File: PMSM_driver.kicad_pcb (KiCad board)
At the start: 2 copper layers, 81 parts, among them J1 22-23-2021, J2 302-S101, J3 Conn_Bridge_Power, J4 Conn_Phases, J5 Conn_Driver_Power, Q1 IRFH8334, Q2 IRFH8334, Q3 IRFH8334, Q4 IRFH8334, Q5 IRFH8334, Q6 IRFH8334, U1 IR2110, U2 IR2110, U3 IR2110, U4 LM358DT

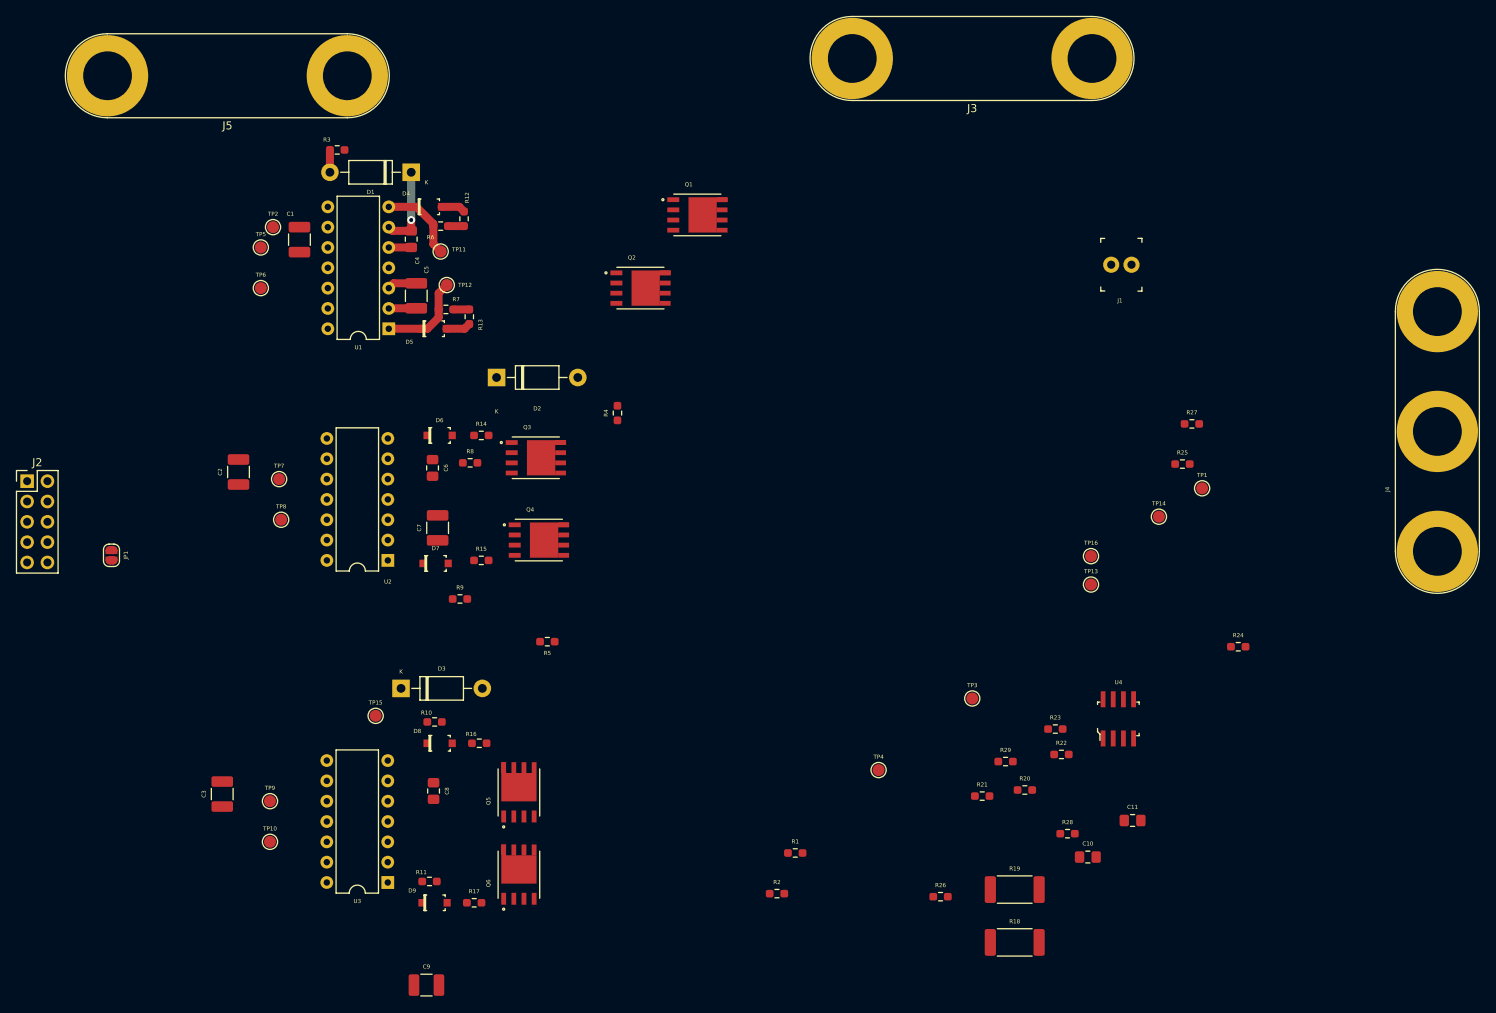
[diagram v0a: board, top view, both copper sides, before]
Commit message: [PCB]: components arrangment around 3 MOSFET drivers
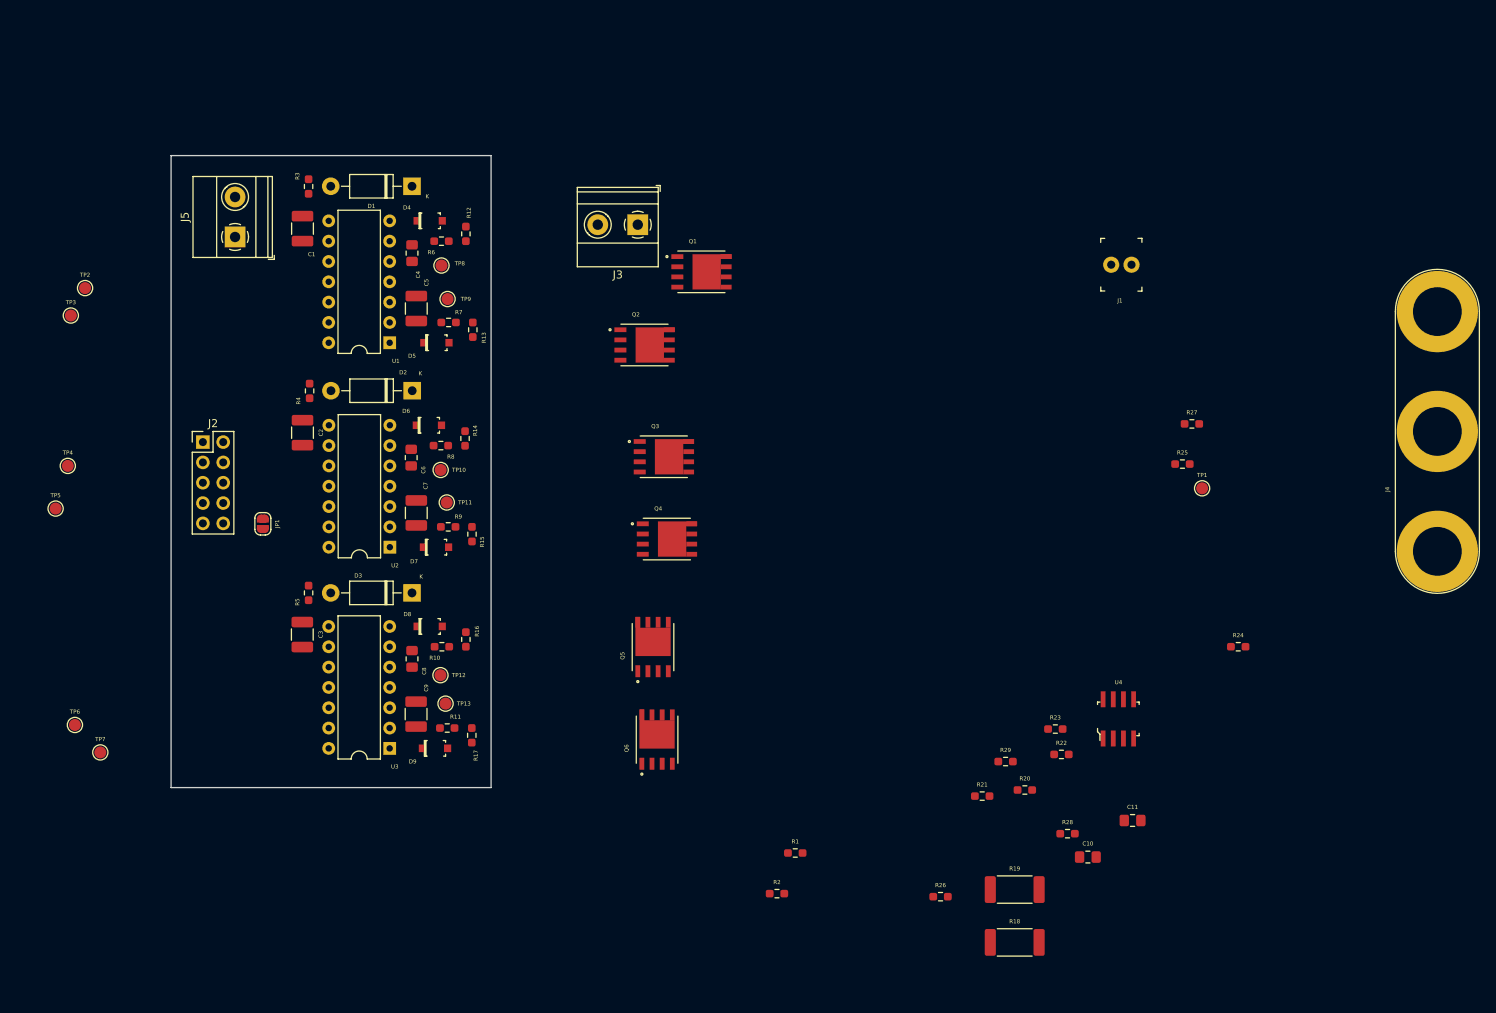
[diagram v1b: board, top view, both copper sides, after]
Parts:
- removed the TP2 at (110.7, 59.9)
- removed the TP3 at (198.2, 118.9)
- removed the TP4 at (186.4, 127.8)
- J3: value Conn_Bridge_Power -> Screw_Terminal_Power; footprint Connector:Banana_Jack_2Pin -> TerminalBlock_Phoenix:TerminalBlock_Phoenix_MKDS-1,5-2_1x02_P5.00mm_Horizontal
- J5: value Conn_Driver_Power -> Screw_Terminal_Logic; footprint Connector:Banana_Jack_2Pin -> TerminalBlock_Phoenix:TerminalBlock_Phoenix_MKDS-1,5-2_1x02_P5.00mm_Horizontal
- moved TP11 89.0 mm to (132.5, 94.4)
- moved TP13 82.8 mm to (132.3, 119.5)
- moved TP10 82.5 mm to (131.7, 90.3)
- moved J3 60.5 mm to (156.3, 59.6)
- moved R4 38.6 mm to (115.3, 80.4)
- moved C9 33.9 mm to (128.6, 120.8), turned to 90 degrees
- moved R5 30.5 mm to (115.2, 105.7), turned to 90 degrees
- moved TP5 28.2 mm to (83.6, 95.1)
- moved TP4 26.5 mm to (85.1, 89.8)
- moved TP6 26.2 mm to (86.0, 122.2)
- moved Q5 24.7 mm to (158.2, 112.4)
- moved J5 24.6 mm to (106.0, 61.2), turned to 90 degrees
- moved Q6 24.2 mm to (158.8, 124.0)
- moved TP3 24.0 mm to (85.5, 71.0)
- moved TP7 24.0 mm to (89.2, 125.6)
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- renumbered TP13 to TP10, TP14 to TP11, TP15 to TP12, TP16 to TP13, TP5 to TP2, TP6 to TP3, TP7 to TP4, TP8 to TP5, TP9 to TP6, TP10 to TP7, TP11 to TP8, TP12 to TP9
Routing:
- net Net-(D5-PadK): track 11.3 -> 0.00 mm
- net Net-(C4-Pad1): track 10.3 -> 0.00 mm, vias 1 -> 0
- net Net-(D4-PadK): track 10.3 -> 0.00 mm
- net VCC: track 3.69 -> 0.00 mm
- net GND: track 3.45 -> 0.00 mm
- net Net-(D5-PadA): track 3.11 -> 0.00 mm
- net Net-(D4-PadA): track 3.06 -> 0.00 mm
- net Net-(C4-Pad2): track 2.81 -> 0.00 mm
- net Net-(D1-Pad2): track 2.79 -> 0.00 mm
- net Net-(Q2-Pad4): track 2.01 -> 0.00 mm
- net Net-(Q1-Pad4): track 2.01 -> 0.00 mm
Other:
- board outline added: 40 x 79 mm

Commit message: [PCB]: added Power part of the board. Logic part rearrangement
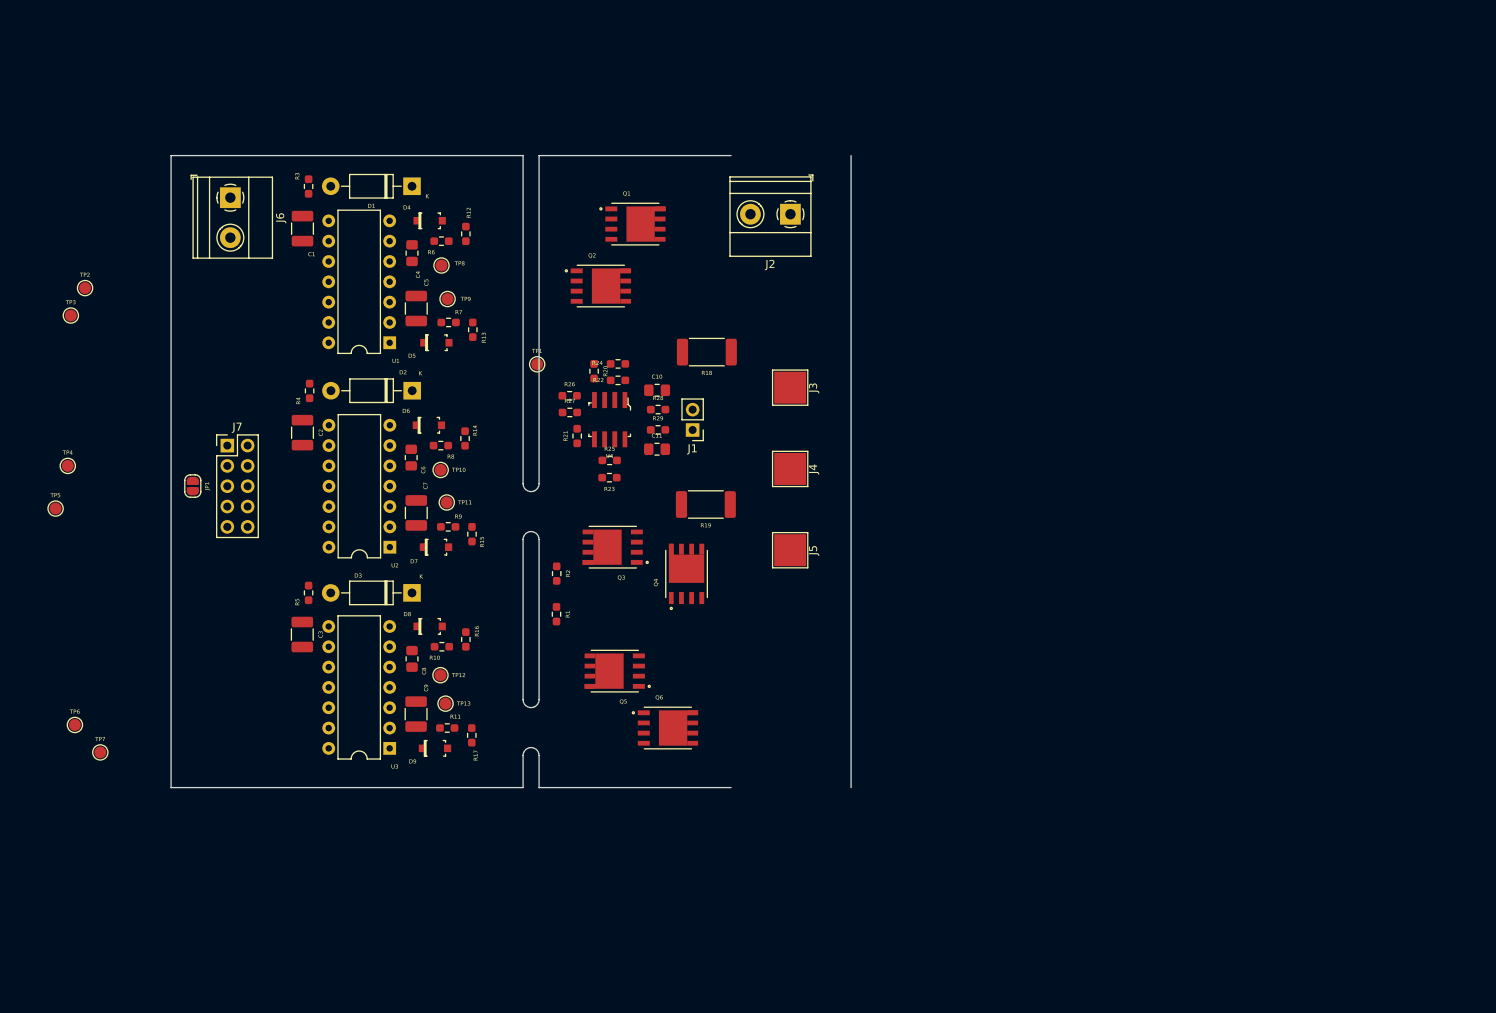
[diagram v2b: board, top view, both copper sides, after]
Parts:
- added J3: Screw_Terminal_1, TestPoint:TestPoint_Pad_4.0x4.0mm, F.Cu at (175.4, 80.0)
- added J5: Screw_Terminal_3, TestPoint:TestPoint_Pad_4.0x4.0mm, F.Cu at (175.4, 100.3)
- J1: footprint digikey-footprints:PinHeader_1x2_P2.54mm_Drill1.02mm -> Connector_PinHeader_2.54mm:PinHeader_1x02_P2.54mm_Vertical
- J4: value Conn_Phases -> Screw_Terminal_2; footprint Connector:Banana_Jack_3Pin -> TestPoint:TestPoint_Pad_4.0x4.0mm
- moved TP1 84.5 mm to (143.8, 77.1)
- moved R24 84.4 mm to (153.9, 79.1)
- moved R18 83.2 mm to (165.0, 75.6), turned to 180 degrees
- moved J4 81.6 mm to (175.4, 90.2), turned to -90 degrees
- moved C10 79.4 mm to (158.8, 80.3)
- moved R26 77.9 mm to (147.8, 81.0)
- moved R27 77.8 mm to (147.8, 83.1)
- moved C11 75.4 mm to (158.7, 87.7)
- moved R20 75.1 mm to (150.9, 78.0), turned to -90 degrees
- moved R22 73.9 mm to (153.9, 77.0), turned to 180 degrees
- moved U4 73.8 mm to (152.8, 84.0), turned to 180 degrees
- moved R28 73.7 mm to (158.9, 82.7)
- moved R25 71.6 mm to (152.8, 89.1)
- moved R21 67.7 mm to (148.8, 86.1), turned to 90 degrees
- moved R23 64.0 mm to (152.8, 91.3), turned to 180 degrees
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- renumbered J3 to J2, J5 to J6, J2 to J7
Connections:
- J4 pad 1: PHASE_1 -> PHASE_2
- J7 pad 1: /L1 -> /H1
- J7 pad 10: +3.3V -> /H3
- J7 pad 2: /H1 -> /L1
- J7 pad 3: /L2 -> VDD
- J7 pad 5: /L3 -> GND
- J7 pad 6: /H3 -> GND
- J7 pad 7: GND -> +3.3V
- J7 pad 8: VDD -> /L2
- J7 pad 9: GND -> /L3
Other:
- board size 40 x 79 mm -> 85 x 79 mm

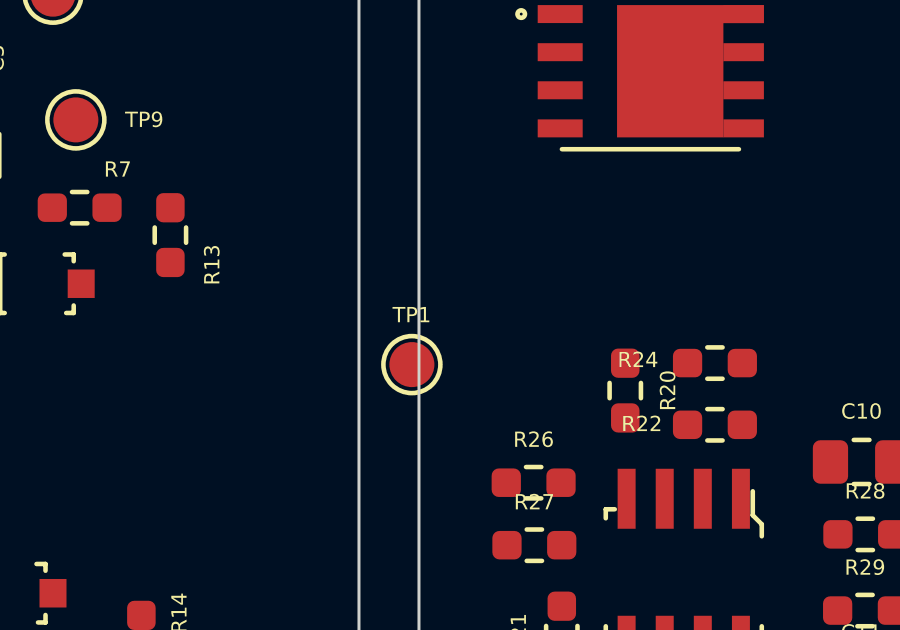
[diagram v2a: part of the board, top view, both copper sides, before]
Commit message: [PCB]: update panelization libs
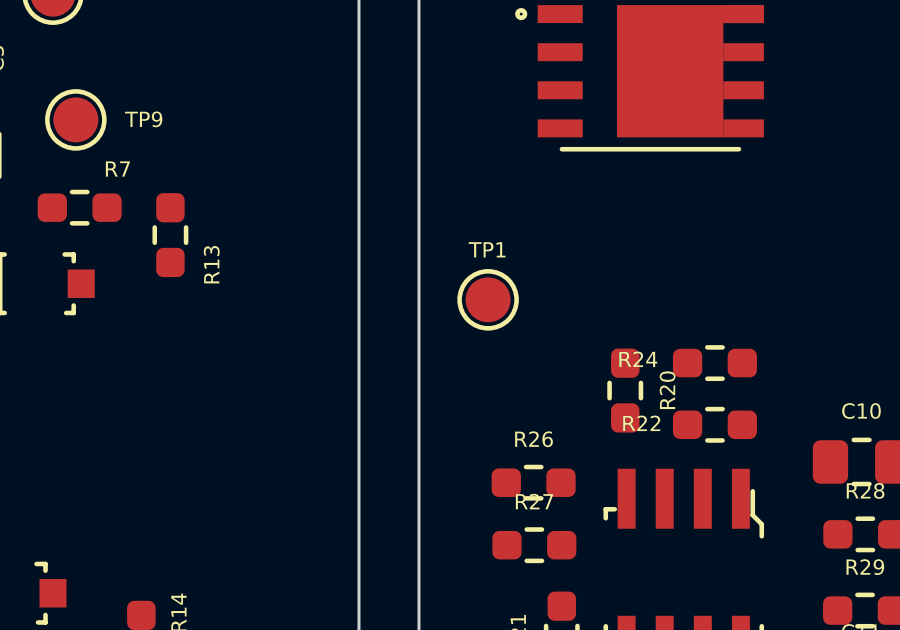
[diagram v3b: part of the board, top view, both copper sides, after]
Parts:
- moved TP1 3.33 mm to (146.3, 74.9)
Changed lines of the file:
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@@
   )
   (footprint "TestPoint:TestPoint_Pad_D1.5mm" (layer "F.Cu")
-    (at 143.764 77.089)
+    (at 146.304 74.93)
     (descr "SMD pad as test Point, diameter 1.5mm")
     (tags "test point SMD pad")

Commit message: [PCB]: Mosfets rearrangement
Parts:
- Q1: moved to B.Cu
- moved J2 21.4 mm to (154.0, 58.1)
- moved Q1 7.96 mm to (159.6, 66.7)
- moved Q2 2.55 mm to (154.3, 67.6)
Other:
- outline, holes or cut-outs redrawn

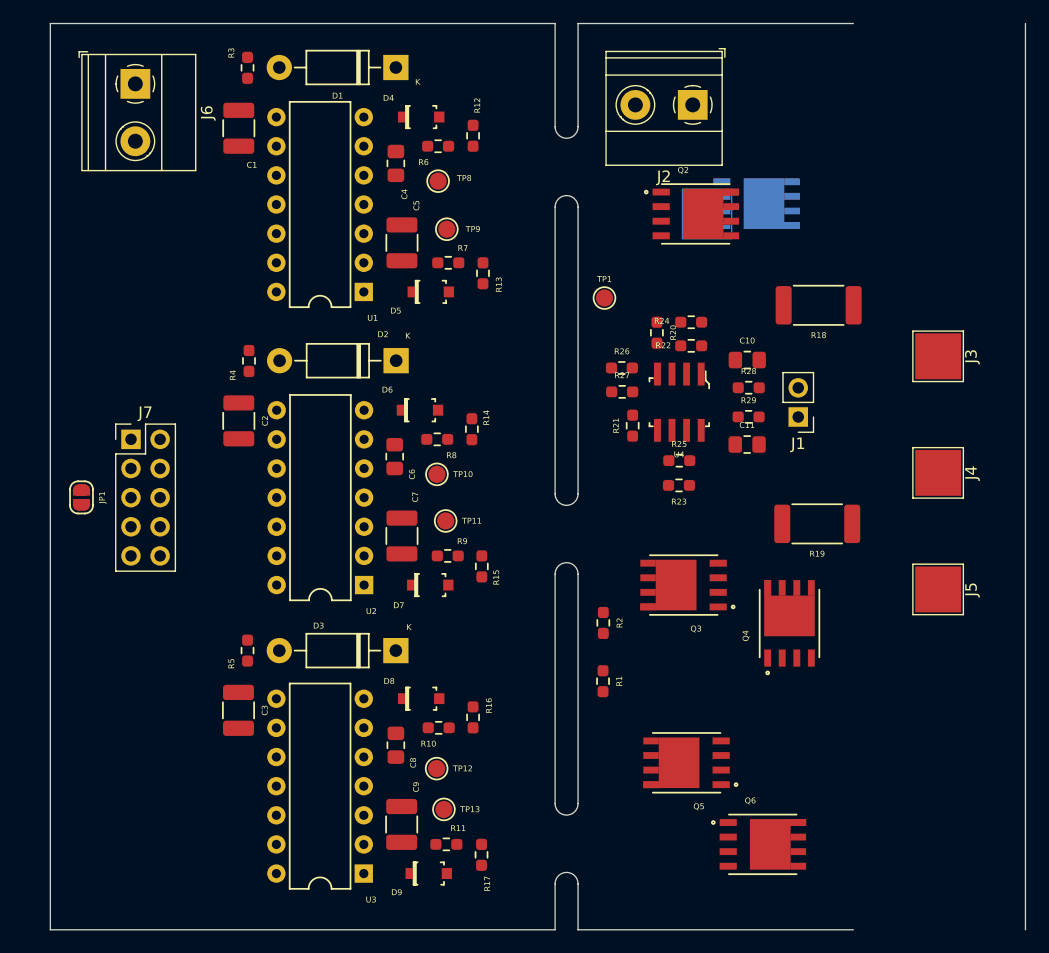
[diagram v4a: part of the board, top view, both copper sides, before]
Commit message: [PCB]: size optimization
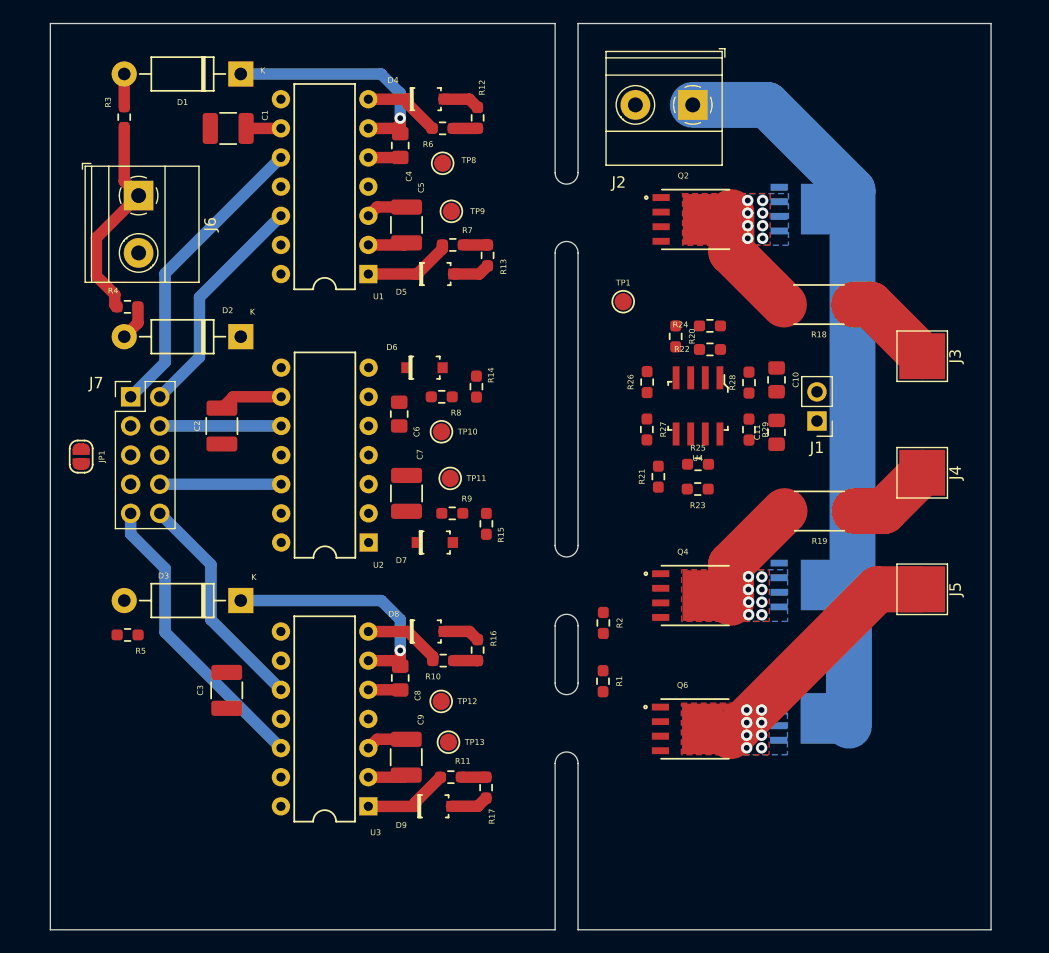
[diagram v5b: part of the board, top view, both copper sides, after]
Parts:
- Q3, Q5: moved to B.Cu
- moved D3 14.2 mm to (114.6, 101.3)
- moved D2 13.7 mm to (114.6, 78.3)
- moved D1 13.5 mm to (114.6, 55.4)
- moved Q5 11.8 mm to (164.6, 111.6), turned to 0 degrees
- moved Q6 11.7 mm to (154.2, 112.5)
- moved R4 11.6 mm to (104.7, 75.7), turned to 0 degrees
- moved R3 11.6 mm to (104.4, 59.2)
- moved Q3 11.4 mm to (164.6, 99.9), turned to 0 degrees
- moved R5 10.5 mm to (104.7, 104.3), turned to 180 degrees
- moved J6 9.74 mm to (105.7, 66.0)
- moved Q4 8.51 mm to (154.3, 100.9), turned to 0 degrees
- moved R11 5.87 mm to (132.9, 116.7)
- moved C9 5.87 mm to (129.0, 115.0)
- moved D8 5.87 mm to (130.7, 104.0)
- moved D9 5.87 mm to (131.4, 119.2)
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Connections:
- net Net-(C4-Pad2) renamed /Q1_Q2
- net Net-(C6-Pad2) renamed /Q3_Q4
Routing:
- net +VDC: track 0.00 -> 63.8 mm
- net /H1: track 0.00 -> 26.3 mm
- net /L3: track 0.00 -> 25.9 mm
- net VCC: track 0.00 -> 25.7 mm
- net PHASE_3: track 0.00 -> 24.8 mm, vias 0 -> 8
- net Net-(C8-Pad1): track 0.00 -> 21.6 mm, vias 0 -> 1
- net Net-(C4-Pad1): track 0.00 -> 21.1 mm, vias 0 -> 1
- net /L1: track 0.00 -> 20.2 mm
- net /H3: track 0.00 -> 19.8 mm
- net /Q1_Q2: track 0.00 -> 12.7 mm, vias 0 -> 8
- net /L2: track 0.00 -> 10.6 mm
- net /H2: track 0.00 -> 10.6 mm
- net /Q3_Q4: track 0.00 -> 9.94 mm, vias 0 -> 8
- net VDD: track 0.00 -> 8.63 mm
- net PHASE_1: track 0.00 -> 7.81 mm
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- added copper zone on B.Cu, net /Q1_Q2
- added copper zone on F.Cu, net /Q1_Q2
- added copper zone on B.Cu, net /Q3_Q4
- added copper zone on F.Cu, net /Q3_Q4
- added copper zone on B.Cu, net PHASE_3
- added copper zone on F.Cu, net PHASE_3
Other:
- board size 85 x 79 mm -> 82 x 79 mm
